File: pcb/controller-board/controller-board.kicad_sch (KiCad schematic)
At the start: 10 parts, among them J10 PWR_IN, J2 CAN, U1 STM32G474RETx, U2 AMS1117-3.3, U3 SN65HVD230

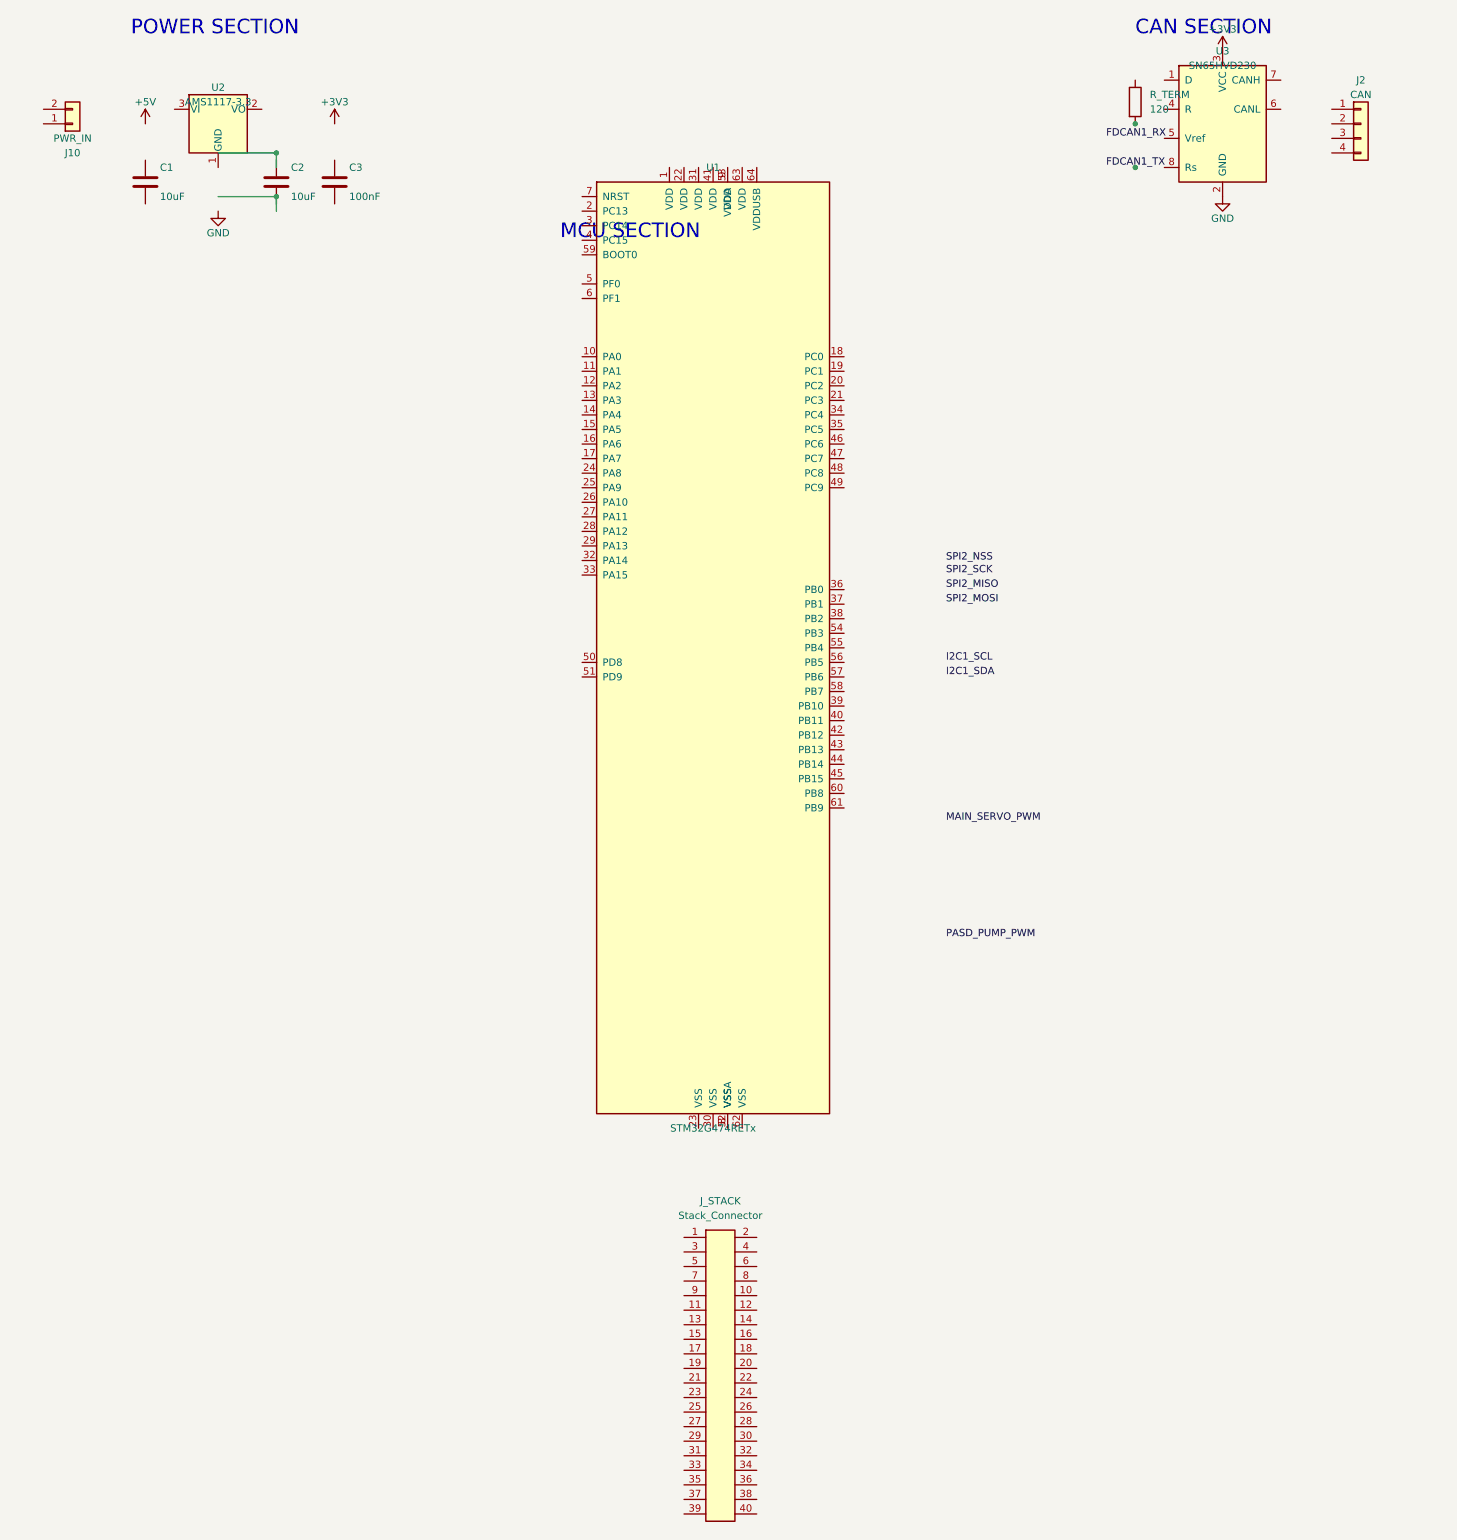
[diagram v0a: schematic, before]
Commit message: Update KiCAD controller board files and add schematic generator script
Co-Authored-By: Claude Opus 4.6 <noreply@anthropic.com>
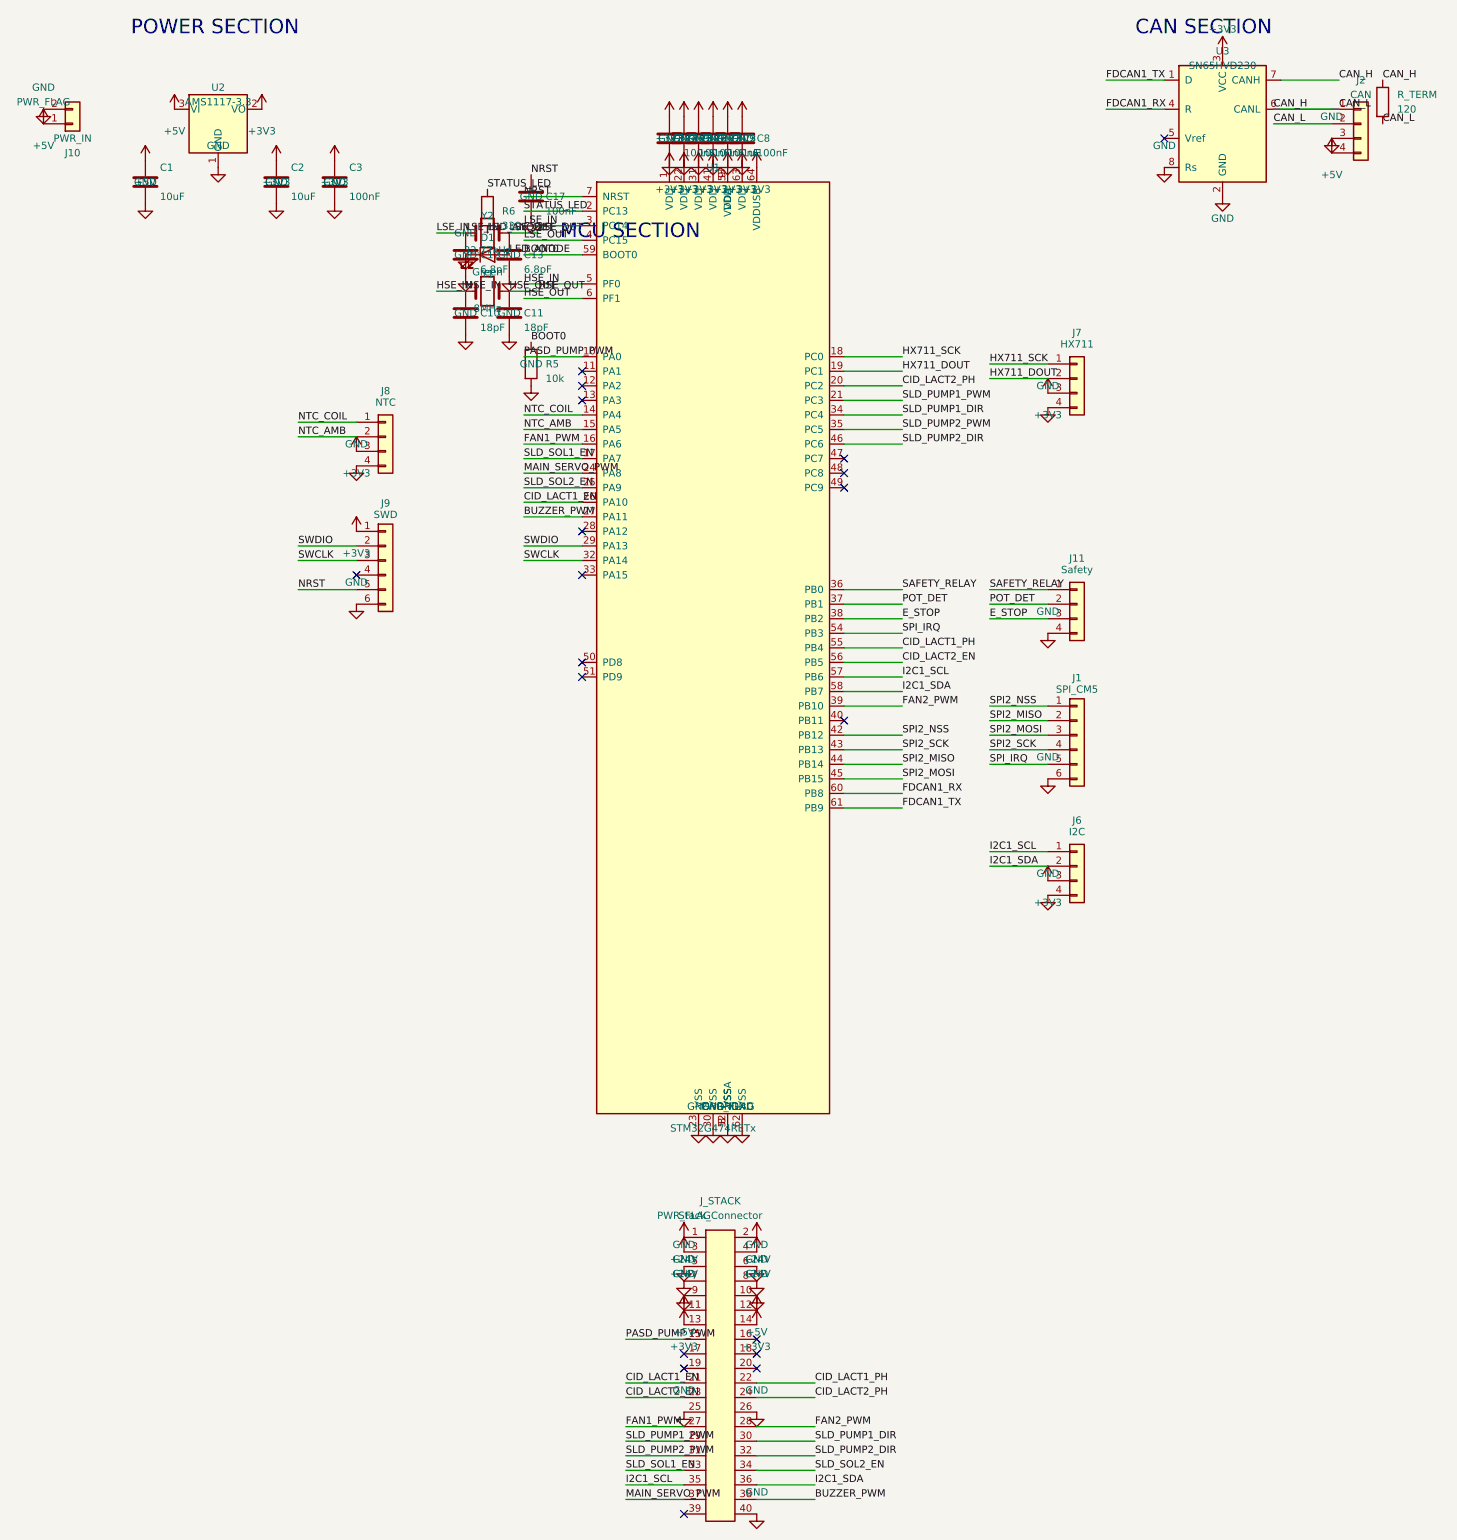
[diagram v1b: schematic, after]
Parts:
- added C10, C11: 18pF, Capacitor_SMD:C_0402_1005Metric, symbol Device:C
- added C12, C13: 6.8pF, Capacitor_SMD:C_0402_1005Metric, symbol Device:C
- added C17, C4, C5, C6, C7, C8: 100nF, Capacitor_SMD:C_0402_1005Metric, symbol Device:C
- added C9: 1uF, Capacitor_SMD:C_0402_1005Metric, symbol Device:C
- added D1: Green, LED_SMD:LED_0603_1608Metric, symbol Device:LED
- added J1: SPI_CM5, Connector_JST:JST_SH_BM06B-SRSS-TB_1x06-1MP_P1.00mm_Vertical, symbol Connector_Generic:Conn_01x06
- added J11: Safety, Connector_JST:JST_XH_B4B-XH-A_1x04_P2.50mm_Vertical, symbol Connector_Generic:Conn_01x04
- added J6: I2C, Connector_JST:JST_SH_BM04B-SRSS-TB_1x04-1MP_P1.00mm_Vertical, symbol Connector_Generic:Conn_01x04
- added J7: HX711, Connector_JST:JST_XH_B4B-XH-A_1x04_P2.50mm_Vertical, symbol Connector_Generic:Conn_01x04
- added J8: NTC, Connector_JST:JST_XH_B4B-XH-A_1x04_P2.50mm_Vertical, symbol Connector_Generic:Conn_01x04
- added J9: SWD, Connector_PinHeader_2.54mm:PinHeader_2x05_P2.54mm_Vertical, symbol Connector_Generic:Conn_01x06
- added R5: 10k, Resistor_SMD:R_0402_1005Metric, symbol Device:R
- added R6: 330, Resistor_SMD:R_0402_1005Metric, symbol Device:R
- added Y1: 8MHz, Crystal:Crystal_SMD_HC49-SD, symbol Device:Crystal
- added Y2: 32.77kHz, Crystal:Crystal_SMD_2012-2Pin_2.0x1.2mm, symbol Device:Crystal
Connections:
- net +3V3: now also C2.1, C3.1, J_STACK.13, J_STACK.14, U1.1 (VDD), U1.22 (VDD), U1.31 (VDD), U1.41 (VDD), U1.53 (VDD), U1.63 (VDD), U1.64 (VDDUSB), U1.9 (VDDA), U2.2 (VO), C4.1, C5.1, C6.1, C7.1, C8.1, C9.1, J6.3 (Pin_3), J7.3 (Pin_3), J8.3 (Pin_3), J9.1 (Pin_1)
- net +5V: now also C1.1, J10.1 (Pin_1), J2.4 (Pin_4), J_STACK.11, J_STACK.12, U2.3 (VI)
- net FDCAN1_RX: now also U1.60 (PB8), U3.4 (R)
- net FDCAN1_TX: now also U1.61 (PB9), U3.1 (D)
- net GND: now also C1.2, C2.2, C3.2, J10.2 (Pin_2), J2.3 (Pin_3), J_STACK.10, J_STACK.25, J_STACK.26, J_STACK.40, J_STACK.5, J_STACK.6, J_STACK.7, J_STACK.8, J_STACK.9, U1.23 (VSS), U1.30 (VSS), U1.52 (VSS), U1.62 (VSS), U1.8 (VSSA), U2.1 (GND), U3.8 (Rs), C10.2, C11.2, C12.2, C13.2, C17.2, C4.2, C5.2, C6.2, C7.2, C8.2, C9.2, D1.1 (K), J1.6 (Pin_6), J11.4 (Pin_4), J6.4 (Pin_4), J7.4 (Pin_4), J8.4 (Pin_4), J9.6 (Pin_6), R5.2
- net I2C1_SCL: now also J_STACK.35, U1.57 (PB6), J6.1 (Pin_1)
- net I2C1_SDA: now also J_STACK.36, U1.58 (PB7), J6.2 (Pin_2)
- net MAIN_SERVO_PWM: now also J_STACK.37, U1.24 (PA8)
- net PASD_PUMP_PWM: now also J_STACK.15, U1.10 (PA0)
- net SPI2_MISO: now also U1.44 (PB14), J1.2 (Pin_2)
- net SPI2_MOSI: now also U1.45 (PB15), J1.3 (Pin_3)
- net SPI2_NSS: now also U1.42 (PB12), J1.1 (Pin_1)
- net SPI2_SCK: now also U1.43 (PB13), J1.4 (Pin_4)
- net CAN_H: now reaches J2.1 (Pin_1)
- net CAN_H: now also J2.2 (Pin_2), R_TERM.1, R_TERM.2, U3.6 (CANL), U3.7 (CANH)
- net +24V: now reaches J_STACK.1
- net +24V: now also J_STACK.2, J_STACK.3, J_STACK.4
- net CID_LACT1_EN: now reaches J_STACK.21
- net CID_LACT1_EN: now also U1.26 (PA10)
- net CID_LACT1_PH: now reaches J_STACK.22
- net CID_LACT1_PH: now also U1.55 (PB4)
- net CID_LACT2_EN: now reaches J_STACK.23
- net CID_LACT2_EN: now also U1.56 (PB5)
- net CID_LACT2_PH: now reaches J_STACK.24
- net CID_LACT2_PH: now also U1.20 (PC2)
- net FAN1_PWM: now reaches J_STACK.27
- net FAN1_PWM: now also U1.16 (PA6)
- net FAN2_PWM: now reaches J_STACK.28
- net FAN2_PWM: now also U1.39 (PB10)
- net SLD_PUMP1_PWM: now reaches J_STACK.29
- net SLD_PUMP1_PWM: now also U1.21 (PC3)
- net SLD_PUMP1_DIR: now reaches J_STACK.30
- net SLD_PUMP1_DIR: now also U1.34 (PC4)
- net SLD_PUMP2_PWM: now reaches J_STACK.31
- net SLD_PUMP2_PWM: now also U1.35 (PC5)
- net SLD_PUMP2_DIR: now reaches J_STACK.32
- net SLD_PUMP2_DIR: now also U1.46 (PC6)
- net SLD_SOL1_EN: now reaches J_STACK.33
- net SLD_SOL1_EN: now also U1.17 (PA7)
- net SLD_SOL2_EN: now reaches J_STACK.34
- net SLD_SOL2_EN: now also U1.25 (PA9)
- net BUZZER_PWM: now reaches J_STACK.38
- net BUZZER_PWM: now also U1.27 (PA11)
- net NTC_COIL: now reaches U1.14 (PA4)
- net NTC_COIL: now also J8.1 (Pin_1)
- net NTC_AMB: now reaches U1.15 (PA5)
- net NTC_AMB: now also J8.2 (Pin_2)
- net HX711_SCK: now reaches U1.18 (PC0)
- net HX711_SCK: now also J7.1 (Pin_1)
- net HX711_DOUT: now reaches U1.19 (PC1)
- net HX711_DOUT: now also J7.2 (Pin_2)
- net STATUS_LED: now reaches U1.2 (PC13)
- net STATUS_LED: now also R6.1
- net SWDIO: now reaches U1.29 (PA13)
- net SWDIO: now also J9.2 (Pin_2)
- net LSE_IN: now reaches U1.3 (PC14)
- net LSE_IN: now also C12.1, Y2.1
- net SWCLK: now reaches U1.32 (PA14)
- net SWCLK: now also J9.3 (Pin_3)
- net SAFETY_RELAY: now reaches U1.36 (PB0)
- net SAFETY_RELAY: now also J11.1 (Pin_1)
- net POT_DET: now reaches U1.37 (PB1)
- net POT_DET: now also J11.2 (Pin_2)
- net E_STOP: now reaches U1.38 (PB2)
- net E_STOP: now also J11.3 (Pin_3)
- net LSE_OUT: now reaches U1.4 (PC15)
- net LSE_OUT: now also C13.1, Y2.2
- net HSE_IN: now reaches U1.5 (PF0)
- net HSE_IN: now also C10.1, Y1.1
- net SPI_IRQ: now reaches U1.54 (PB3)
- net SPI_IRQ: now also J1.5 (Pin_5)
- net BOOT0: now reaches U1.59 (BOOT0)
- net BOOT0: now also R5.1
- net HSE_OUT: now reaches U1.6 (PF1)
- net HSE_OUT: now also C11.1, Y1.2
- net NRST: now reaches U1.7 (NRST)
- net NRST: now also C17.1, J9.5 (Pin_5)
- new net LED_ANODE: D1.2 (A), R6.2
- no-connect marks 0 -> 19
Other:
- moved on the sheet: R_TERM
